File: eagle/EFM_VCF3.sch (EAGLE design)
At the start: 44 parts, among them IC1 LM13700N, IC2 TL084P, Q3 2N3906, Q4 2N3906, U1 POWER

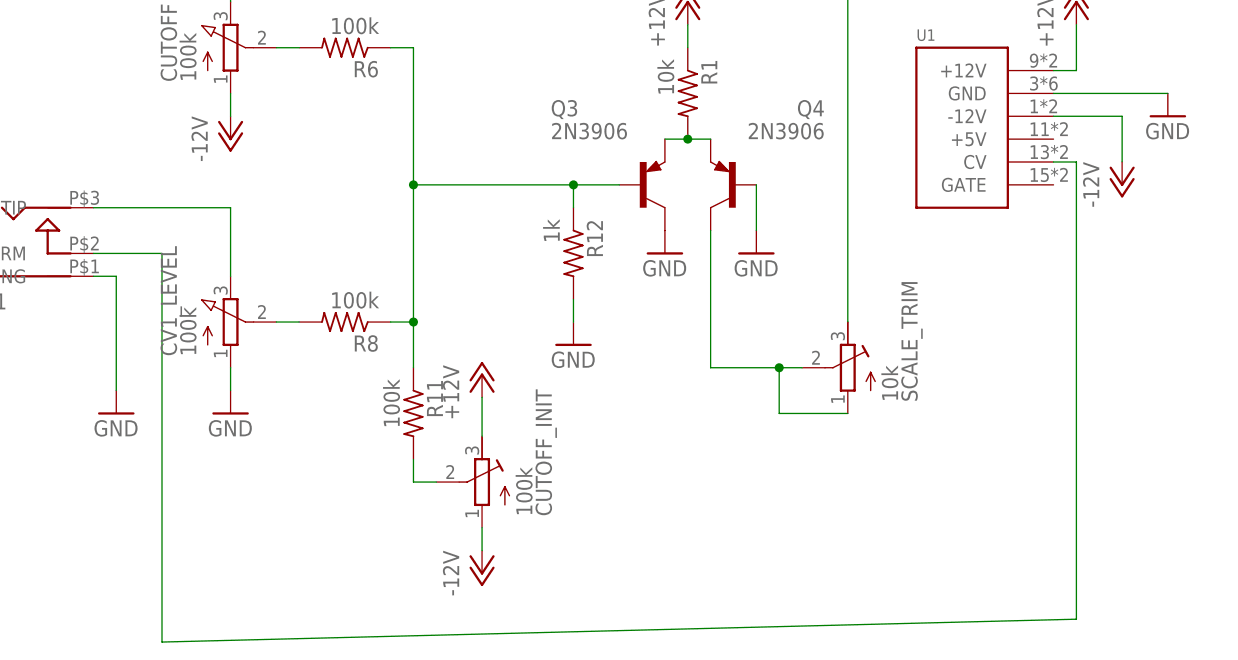
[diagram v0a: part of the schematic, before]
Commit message: gcode for rectangular cut
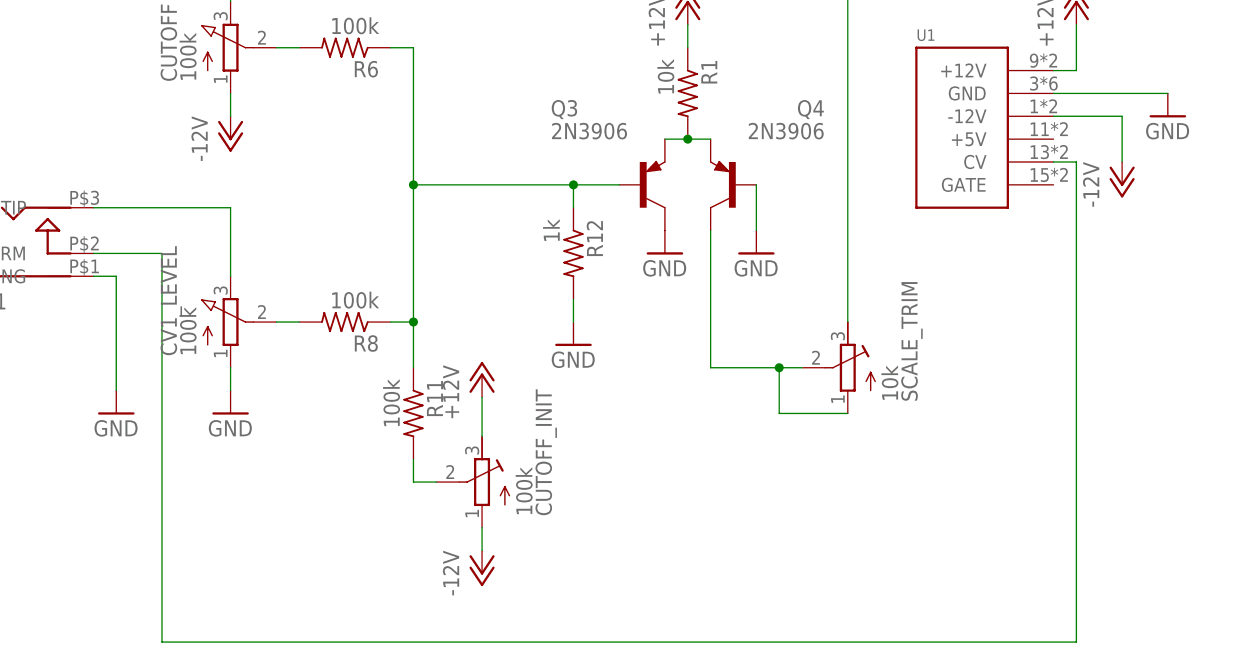
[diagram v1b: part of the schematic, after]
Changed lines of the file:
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@@
 <?xml version="1.0" encoding="utf-8"?>
 <!DOCTYPE eagle SYSTEM "eagle.dtd">
-<eagle version="7.1.0">
+<eagle version="7.6.0">
 <drawing>
 <settings>
@@
 <pinref part="U1" gate="G$1" pin="CV"/>
 <wire x1="45.72" y1="33.02" x2="48.26" y2="33.02" width="0.1524" layer="91"/>
-<wire x1="48.26" y1="33.02" x2="48.26" y2="-17.78" width="0.1524" layer="91"/>
-<wire x1="48.26" y1="-17.78" x2="-53.34" y2="-20.32" width="0.1524" layer="91"/>
+<wire x1="48.26" y1="33.02" x2="48.26" y2="-20.32" width="0.1524" layer="91"/>
+<wire x1="48.26" y1="-20.32" x2="-53.34" y2="-20.32" width="0.1524" layer="91"/>
 <wire x1="-53.34" y1="-20.32" x2="-53.34" y2="22.86" width="0.1524" layer="91"/>
 <pinref part="CV_1" gate="G$1" pin="NORM"/>
